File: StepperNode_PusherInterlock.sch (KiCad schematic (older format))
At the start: 12 parts, among them P4 TE_640456-8, P5 TE_640456-8, U4 MAX3232CDR, U5 MAX3232CDR

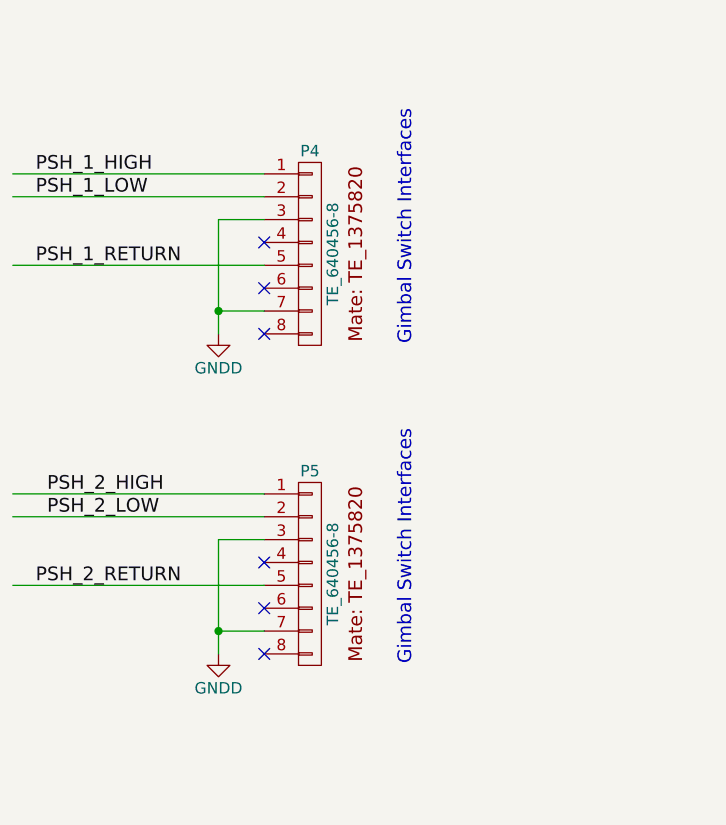
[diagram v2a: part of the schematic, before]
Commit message: Finish isolation and add brake limit switches.
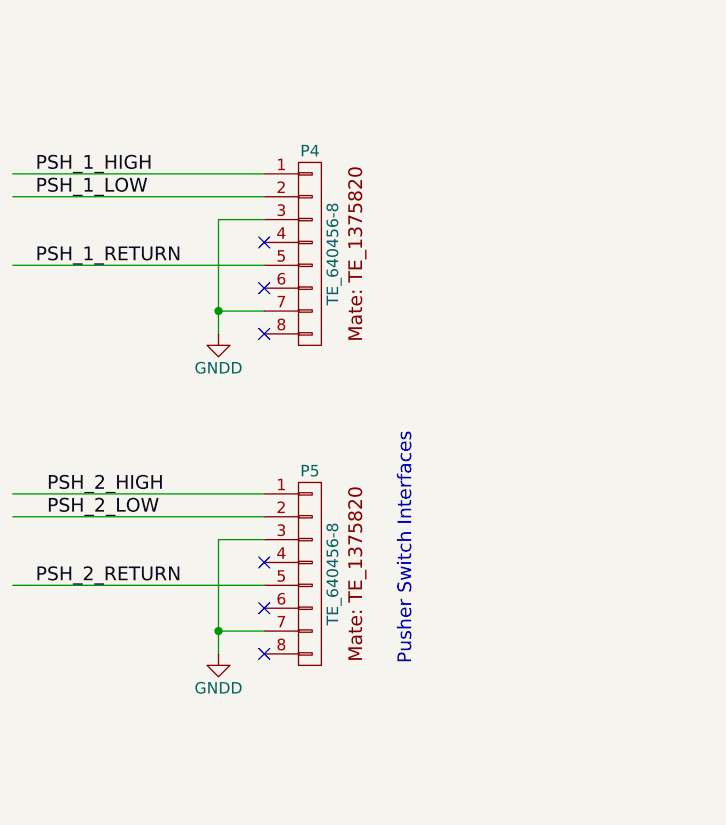
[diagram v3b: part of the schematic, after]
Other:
- note added: "Pusher Switch Interfaces"
- note removed: "Gimbal Switch Interfaces"
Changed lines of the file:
@@
 Text Notes 11950 10500 0    60   ~ 0
 Original Author: SafetyLok
-Text Notes 13500 3550 1    60   ~ 0
-Gimbal Switch Interfaces
-$Comp
-L GNDD #PWR025
+$Comp
+L GNDD #PWR74
 U 1 1 575DC471
 P 12650 3500
-F 0 "#PWR025" H 12650 3250 50  0001 C CNN
+F 0 "#PWR74" H 12650 3250 50  0001 C CNN
 F 1 "GNDD" H 12650 3350 50  0000 C CNN
 F 2 "" H 12650 3500 50  0000 C CNN
@@
 	11750 3200 12850 3200
 Text Notes 13500 4950 1    60   ~ 0
-Gimbal Switch Interfaces
-$Comp
-L GNDD #PWR026
+Pusher Switch Interfaces
+$Comp
+L GNDD #PWR75
 U 1 1 575DC497
 P 12650 4900
-F 0 "#PWR026" H 12650 4650 50  0001 C CNN
+F 0 "#PWR75" H 12650 4650 50  0001 C CNN
 F 1 "GNDD" H 12650 4750 50  0000 C CNN
 F 2 "" H 12650 4900 50  0000 C CNN
@@
 	11750 4600 12850 4600
 $Comp
-L GNDD #PWR027
+L GNDD #PWR69
 U 1 1 575DC4D0
 P 5300 5100
-F 0 "#PWR027" H 5300 4850 50  0001 C CNN
+F 0 "#PWR69" H 5300 4850 50  0001 C CNN
 F 1 "GNDD" H 5300 4950 50  0000 C CNN
 F 2 "" H 5300 5100 50  0000 C CNN
@@
 	5650 5100 5650 4800
 $Comp
-L +3V3_A #PWR028
+L +3V3_A #PWR68
 U 1 1 575DC4D8
 P 5300 2450
-F 0 "#PWR028" H 5300 2300 50  0001 C CNN
+F 0 "#PWR68" H 5300 2300 50  0001 C CNN
 F 1 "+3V3_A" H 5300 2590 50  0000 C CNN
 F 2 "" H 5300 2450 60  0000 C CNN
@@
 	4550 3650 4550 3450
 $Comp
-L GNDD #PWR029
+L GNDD #PWR66
 U 1 1 575DC4E6
 P 4950 3900
-F 0 "#PWR029" H 4950 3650 50  0001 C CNN
+F 0 "#PWR66" H 4950 3650 50  0001 C CNN
 F 1 "GNDD" H 4950 3750 50  0000 C CNN
 F 2 "" H 4950 3900 50  0000 C CNN
@@
 	6400 3900 7550 3900
 $Comp
-L GNDD #PWR030
+L GNDD #PWR72
 U 1 1 575DC71B
 P 6400 4300
-F 0 "#PWR030" H 6400 4050 50  0001 C CNN
+F 0 "#PWR72" H 6400 4050 50  0001 C CNN
 F 1 "GNDD" H 6400 4150 50  0000 C CNN
 F 2 "" H 6400 4300 50  0000 C CNN
@@
 PSH_1_RETURN
 $Comp
-L +3V3_A #PWR031
+L +3V3_A #PWR64
 U 1 1 575DCA53
 P 4100 3950
-F 0 "#PWR031" H 4100 3800 50  0001 C CNN
+F 0 "#PWR64" H 4100 3800 50  0001 C CNN
 F 1 "+3V3_A" H 4100 4090 50  0000 C CNN
 F 2 "" H 4100 3950 60  0000 C CNN
@@
 PUSH_INTLK_B
 $Comp
-L GNDD #PWR032
+L GNDD #PWR71
 U 1 1 575DCF10
 P 5300 8900
-F 0 "#PWR032" H 5300 8650 50  0001 C CNN
+F 0 "#PWR71" H 5300 8650 50  0001 C CNN
 F 1 "GNDD" H 5300 8750 50  0000 C CNN
 F 2 "" H 5300 8900 50  0000 C CNN
@@
 	5650 8900 5650 8600
 $Comp
-L +3V3_A #PWR033
+L +3V3_A #PWR70
 U 1 1 575DCF18
 P 5300 6250
-F 0 "#PWR033" H 5300 6100 50  0001 C CNN
+F 0 "#PWR70" H 5300 6100 50  0001 C CNN
 F 1 "+3V3_A" H 5300 6390 50  0000 C CNN
 F 2 "" H 5300 6250 60  0000 C CNN
@@
 	4550 7450 4550 7250
 $Comp
-L GNDD #PWR034
+L GNDD #PWR67
 U 1 1 575DCF26
 P 4950 7700
-F 0 "#PWR034" H 4950 7450 50  0001 C CNN
+F 0 "#PWR67" H 4950 7450 50  0001 C CNN
 F 1 "GNDD" H 4950 7550 50  0000 C CNN
 F 2 "" H 4950 7700 50  0000 C CNN
@@
 	6400 7700 7550 7700
 $Comp
-L GNDD #PWR035
+L GNDD #PWR73
 U 1 1 575DCF2E
 P 6400 8100
-F 0 "#PWR035" H 6400 7850 50  0001 C CNN
+F 0 "#PWR73" H 6400 7850 50  0001 C CNN
 F 1 "GNDD" H 6400 7950 50  0000 C CNN
 F 2 "" H 6400 8100 50  0000 C CNN
@@
 	4100 7800 4100 7750
 $Comp
-L +3V3_A #PWR036
+L +3V3_A #PWR65
 U 1 1 575DD2D6
 P 4100 7750
-F 0 "#PWR036" H 4100 7600 50  0001 C CNN
+F 0 "#PWR65" H 4100 7600 50  0001 C CNN
 F 1 "+3V3_A" H 4100 7890 50  0000 C CNN
 F 2 "" H 4100 7750 60  0000 C CNN
